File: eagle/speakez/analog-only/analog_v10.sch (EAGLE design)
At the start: 22 parts, among them U1 +12v

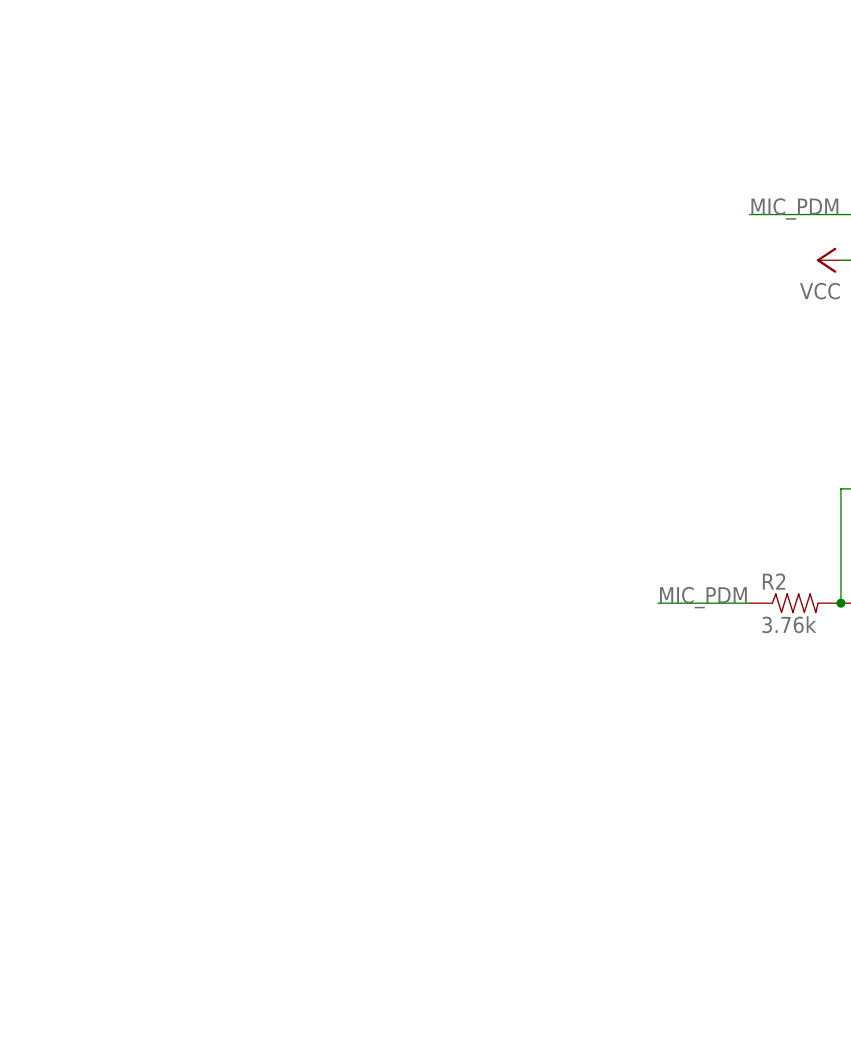
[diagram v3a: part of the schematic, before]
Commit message: added volume control
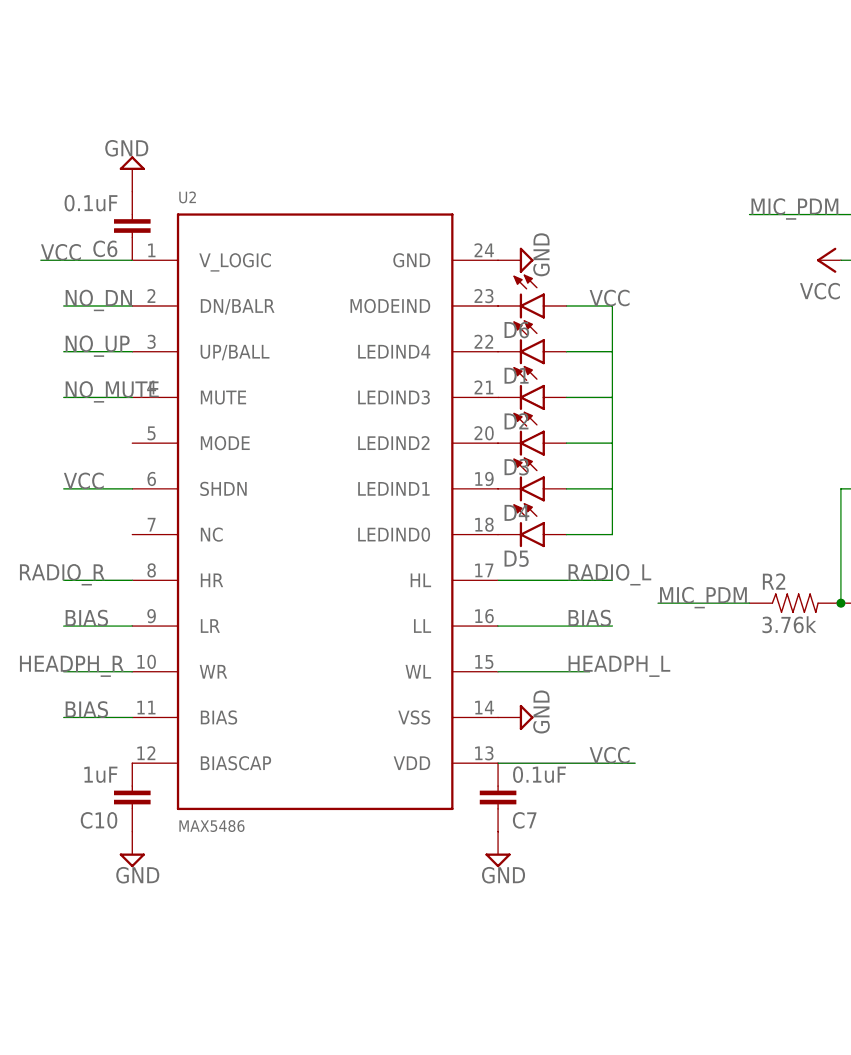
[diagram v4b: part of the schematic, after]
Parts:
- added C10: 1uF, SparkFun-Passives:CAP0805
- added C6, C7: 0.1uF, SparkFun-Passives:CAP0805
- added D1, D2, D3, D4, D5, D6: (no value), SparkFun-LED:LED1206
- added U2: MAX5486, MAX5486:MAX5486
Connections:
- new net BIAS: U2.BIAS, U2.LL, U2.LR
- new net HEADPH_L: U2.WL
- new net HEADPH_R: U2.WR
- new net N$10: D5.C, U2.LEDIND0
- new net N$11: D6.C, U2.MODEIND
- new net N$12: C10.2, U2.BIASCAP
- new net N$5: D1.C, U2.LEDIND4
- new net N$6: D2.C, U2.LEDIND3
- new net N$8: D3.C, U2.LEDIND2
- new net N$9: D4.C, U2.LEDIND1
- new net NO_DN: U2.DN/BALR
- new net NO_MUTE: U2.MUTE
- new net NO_UP: U2.UP/BALL
- new net RADIO_L: U2.HL
- new net RADIO_R: U2.HR
- net GND: now also C10.1, C6.2, C7.1, U2.GND, U2.VSS
- net VCC: now also C6.1, C7.2, D1.A, D2.A, D3.A, D4.A, D5.A, D6.A, U2.SHDN, U2.VDD, U2.V_LOGIC
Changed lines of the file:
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@@
 <part name="RADIO" library="35mm_audio" deviceset="SJ-43514-SMT" device=""/>
 <part name="VD2" library="diode" deviceset="DIODE-SCHOTTKY-" device="SOD123"/>
+<part name="U2" library="MAX5486" deviceset="MAX5486" device=""/>
+<part name="SUPPLY10" library="supply2" deviceset="GND" device=""/>
+<part name="SUPPLY13" library="supply2" deviceset="GND" device=""/>
+<part name="C6" library="SparkFun-Passives" deviceset="CAP" device="0805" value="0.1uF"/>
+<part name="C7" library="SparkFun-Passives" deviceset="CAP" device="0805" value="0.1uF"/>
+<part name="SUPPLY16" library="supply2" deviceset="GND" device=""/>
+<part name="SUPPLY17" library="supply2" deviceset="GND" device=""/>
+<part name="D1" library="SparkFun-LED" deviceset="LED" device="1206"/>
+<part name="D2" library="SparkFun-LED" deviceset="LED" device="1206"/>
+<part name="D3" library="SparkFun-LED" deviceset="LED" device="1206"/>
+<part name="D4" library="SparkFun-LED" deviceset="LED" device="1206"/>
+<part name="D5" library="SparkFun-LED" deviceset="LED" device="1206"/>
+<part name="D6" library="SparkFun-LED" deviceset="LED" device="1206"/>
+<part name="C10" library="SparkFun-Passives" deviceset="CAP" device="0805" value="1uF"/>
+<part name="SUPPLY14" library="supply2" deviceset="GND" device=""/>
 </parts>
 <sheets>
@@
 <instance part="RADIO" gate="G$1" x="83.82" y="12.7"/>
 <instance part="VD2" gate="G$1" x="53.34" y="119.38"/>
+<instance part="U2" gate="G$1" x="-48.26" y="66.04"/>
+<instance part="SUPPLY10" gate="GND" x="-25.4" y="99.06" rot="R90"/>
+<instance part="SUPPLY13" gate="GND" x="-25.4" y="48.26" rot="R90"/>
+<instance part="C6" gate="G$1" x="-68.58" y="104.14" rot="R180"/>
+<instance part="C7" gate="G$1" x="-27.94" y="40.64" rot="MR180"/>
+<instance part="SUPPLY16" gate="GND" x="-27.94" y="33.02"/>
+<instance part="SUPPLY17" gate="GND" x="-68.58" y="109.22" rot="R180"/>
+<instance part="D1" gate="G$1" x="-22.86" y="88.9" rot="R270"/>
+<instance part="D2" gate="G$1" x="-22.86" y="83.82" rot="R270"/>
+<instance part="D3" gate="G$1" x="-22.86" y="78.74" rot="R270"/>
+<instance part="D4" gate="G$1" x="-22.86" y="73.66" rot="R270"/>
+<instance part="D5" gate="G$1" x="-22.86" y="68.58" rot="R270"/>
+<instance part="D6" gate="G$1" x="-22.86" y="93.98" rot="R270"/>
+<instance part="C10" gate="G$1" x="-68.58" y="40.64" rot="R180"/>
+<instance part="SUPPLY14" gate="GND" x="-68.58" y="33.02"/>
 </instances>
 <busses>
@@
 <wire x1="99.06" y1="7.62" x2="99.06" y2="-7.62" width="0.1524" layer="91"/>
 <label x="99.06" y="-7.62" size="1.778" layer="95" rot="R90"/>
+</segment>
+<segment>
+<pinref part="U2" gate="G$1" pin="GND"/>
+<pinref part="SUPPLY10" gate="GND" pin="GND"/>
+</segment>
+<segment>
+<pinref part="U2" gate="G$1" pin="VSS"/>
+<pinref part="SUPPLY13" gate="GND" pin="GND"/>
+</segment>
+<segment>
+<pinref part="C7" gate="G$1" pin="1"/>
+<pinref part="SUPPLY16" gate="GND" pin="GND"/>
+</segment>
+<segment>
+<pinref part="C6" gate="G$1" pin="2"/>
+<pinref part="SUPPLY17" gate="GND" pin="GND"/>
+</segment>
+<segment>
+<pinref part="C10" gate="G$1" pin="1"/>
+<pinref part="SUPPLY14" gate="GND" pin="GND"/>
 </segment>
 </net>
@@
 <wire x1="76.2" y1="119.38" x2="71.12" y2="119.38" width="0.1524" layer="91"/>
 <junction x="71.12" y="119.38"/>
+</segment>
+<segment>
+<pinref part="U2" gate="G$1" pin="V_LOGIC"/>
+<pinref part="C6" gate="G$1" pin="1"/>
+<wire x1="-78.74" y1="99.06" x2="-68.58" y2="99.06" width="0.1524" layer="91"/>
+<label x="-78.74" y="99.06" size="1.778" layer="95"/>
+</segment>
+<segment>
+<pinref part="U2" gate="G$1" pin="VDD"/>
+<pinref part="C7" gate="G$1" pin="2"/>
+<wire x1="-27.94" y1="43.18" x2="-12.7" y2="43.18" width="0.1524" layer="91"/>
+<label x="-17.78" y="43.18" size="1.778" layer="95"/>
+</segment>
+<segment>
+<pinref part="U2" gate="G$1" pin="SHDN"/>
+<wire x1="-68.58" y1="73.66" x2="-76.2" y2="73.66" width="0.1524" layer="91"/>
+<label x="-76.2" y="73.66" size="1.778" layer="95"/>
+</segment>
+<segment>
+<pinref part="D6" gate="G$1" pin="A"/>
+<wire x1="-20.32" y1="93.98" x2="-15.24" y2="93.98" width="0.1524" layer="91"/>
+<wire x1="-15.24" y1="93.98" x2="-15.24" y2="88.9" width="0.1524" layer="91"/>
+<pinref part="D5" gate="G$1" pin="A"/>
+<wire x1="-15.24" y1="88.9" x2="-15.24" y2="83.82" width="0.1524" layer="91"/>
+<wire x1="-15.24" y1="83.82" x2="-15.24" y2="78.74" width="0.1524" layer="91"/>
+<wire x1="-15.24" y1="78.74" x2="-15.24" y2="73.66" width="0.1524" layer="91"/>
+<wire x1="-15.24" y1="73.66" x2="-15.24" y2="68.58" width="0.1524" layer="91"/>
+<wire x1="-15.24" y1="68.58" x2="-20.32" y2="68.58" width="0.1524" layer="91"/>
+<pinref part="D4" gate="G$1" pin="A"/>
+<wire x1="-20.32" y1="73.66" x2="-15.24" y2="73.66" width="0.1524" layer="91"/>
+<pinref part="D3" gate="G$1" pin="A"/>
+<wire x1="-20.32" y1="78.74" x2="-15.24" y2="78.74" width="0.1524" layer="91"/>
+<pinref part="D2" gate="G$1" pin="A"/>
+<wire x1="-20.32" y1="83.82" x2="-15.24" y2="83.82" width="0.1524" layer="91"/>
+<pinref part="D1" gate="G$1" pin="A"/>
+<wire x1="-20.32" y1="88.9" x2="-15.24" y2="88.9" width="0.1524" layer="91"/>
+<label x="-17.78" y="93.98" size="1.778" layer="95"/>
 </segment>
 </net>
@@
 </segment>
 </net>
+<net name="N$5" class="0">
+<segment>
+<pinref part="U2" gate="G$1" pin="LEDIND4"/>
+<pinref part="D1" gate="G$1" pin="C"/>
+</segment>
+</net>
+<net name="N$6" class="0">
+<segment>
+<pinref part="U2" gate="G$1" pin="LEDIND3"/>
+<pinref part="D2" gate="G$1" pin="C"/>
+</segment>
+</net>
+<net name="N$8" class="0">
+<segment>
+<pinref part="U2" gate="G$1" pin="LEDIND2"/>
+<pinref part="D3" gate="G$1" pin="C"/>
+</segment>
+</net>
+<net name="N$9" class="0">
+<segment>
+<pinref part="U2" gate="G$1" pin="LEDIND1"/>
+<pinref part="D4" gate="G$1" pin="C"/>
+</segment>
+</net>
+<net name="N$10" class="0">
+<segment>
+<pinref part="U2" gate="G$1" pin="LEDIND0"/>
+<pinref part="D5" gate="G$1" pin="C"/>
+</segment>
+</net>
+<net name="N$11" class="0">
+<segment>
+<pinref part="U2" gate="G$1" pin="MODEIND"/>
+<pinref part="D6" gate="G$1" pin="C"/>
+</segment>
+</net>
+<net name="N$12" class="0">
+<segment>
+<pinref part="U2" gate="G$1" pin="BIASCAP"/>
+<pinref part="C10" gate="G$1" pin="2"/>
+</segment>
+</net>
+<net name="BIAS" class="0">
+<segment>
+<pinref part="U2" gate="G$1" pin="LR"/>
+<wire x1="-68.58" y1="58.42" x2="-76.2" y2="58.42" width="0.1524" layer="91"/>
+<label x="-76.2" y="58.42" size="1.778" layer="95"/>
+</segment>
+<segment>
+<pinref part="U2" gate="G$1" pin="BIAS"/>
+<wire x1="-68.58" y1="48.26" x2="-76.2" y2="48.26" width="0.1524" layer="91"/>
+<label x="-76.2" y="48.26" size="1.778" layer="95"/>
+</segment>
+<segment>
+<pinref part="U2" gate="G$1" pin="LL"/>
+<wire x1="-27.94" y1="58.42" x2="-15.24" y2="58.42" width="0.1524" layer="91"/>
+<label x="-20.32" y="58.42" size="1.778" layer="95"/>
+</segment>
+</net>
+<net name="RADIO_R" class="0">
+<segment>
+<pinref part="U2" gate="G$1" pin="HR"/>
+<wire x1="-68.58" y1="63.5" x2="-76.2" y2="63.5" width="0.1524" layer="91"/>
+<label x="-81.28" y="63.5" size="1.778" layer="95"/>
+</segment>
+</net>
+<net name="RADIO_L" class="0">
+<segment>
+<pinref part="U2" gate="G$1" pin="HL"/>
+<wire x1="-27.94" y1="63.5" x2="-15.24" y2="63.5" width="0.1524" layer="91"/>
+<label x="-20.32" y="63.5" size="1.778" layer="95"/>
+</segment>
+</net>
+<net name="NO_DN" class="0">
+<segment>
+<pinref part="U2" gate="G$1" pin="DN/BALR"/>
+<wire x1="-68.58" y1="93.98" x2="-76.2" y2="93.98" width="0.1524" layer="91"/>
+<label x="-76.2" y="93.98" size="1.778" layer="95"/>
+</segment>
+</net>
+<net name="NO_UP" class="0">
+<segment>
+<pinref part="U2" gate="G$1" pin="UP/BALL"/>
+<wire x1="-68.58" y1="88.9" x2="-76.2" y2="88.9" width="0.1524" layer="91"/>
+<label x="-76.2" y="88.9" size="1.778" layer="95"/>
+</segment>
+</net>
+<net name="NO_MUTE" class="0">
+<segment>
+<pinref part="U2" gate="G$1" pin="MUTE"/>
+<wire x1="-68.58" y1="83.82" x2="-76.2" y2="83.82" width="0.1524" layer="91"/>
+<label x="-76.2" y="83.82" size="1.778" layer="95"/>
+</segment>
+</net>
+<net name="HEADPH_L" class="0">
+<segment>
+<pinref part="U2" gate="G$1" pin="WL"/>
+<wire x1="-27.94" y1="53.34" x2="-17.78" y2="53.34" width="0.1524" layer="91"/>
+<label x="-20.32" y="53.34" size="1.778" layer="95"/>
+</segment>
+</net>
+<net name="HEADPH_R" class="0">
+<segment>
+<pinref part="U2" gate="G$1" pin="WR"/>
+<wire x1="-68.58" y1="53.34" x2="-76.2" y2="53.34" width="0.1524" layer="91"/>
+<label x="-81.28" y="53.34" size="1.778" layer="95"/>
+</segment>
+</net>
